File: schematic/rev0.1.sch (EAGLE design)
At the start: 28 parts, among them IC1 L293DD, IC2 L293DD, IC3 L293DD, J1 USB_B_PTH, U1 DS1307Z, Y1 32.768kHz, Y2 16MHz

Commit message: finished routing
Added pinout for bipolar stepper motors, need to source small enough stepper for it.
should read datasheets closer to verify H bridge can run on such little voltage (5V stepper?)
Maybe add more decoupling caps for atmega
maybe add through hole for LED's (so you can mount them)
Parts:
- added C7: 1uF, resistor:C-USC0805
- added IC4: L293D, st-microelectronics:L293D
- added LED2, LED3, LED4: (no value), adafruit:LEDCHIPLED_0805
- added Q1: 600mA/40V, SparkFun-DiscreteSemi:TRANS_NPN-MMBT2222AL
- added R3: 10K, resistor:R-US_R0805
- added R4, R5, R6, R7: 330R, resistor:R-US_R0805
- added S1: (no value), SparkFun-Switches:MOMENTARY-SWITCH-SPST-2-SMD-5.2MM
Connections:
- new net D0: IC1.IN1, U$1.PD2(INT2/RXD1)
- new net D1: IC1.IN2, U$1.PD3(INT3/TXD1)
- new net D10: IC3.IN1, U$1.PB6(OC1B/OC4B/ADC13)
- new net D11: IC3.IN2, U$1.PB7(OC0A/OC1C/RTS)
- new net D12: IC3.IN3, U$1.PD6(T1/ADC9/!OC4D)
- new net D13: IC3.IN4, U$1.PC7(ICP3/CLK0/OC4A)
- new net D4: IC1.IN3, U$1.PD4(ICP1/ADC8)
- new net D5: IC1.IN4, U$1.PC6(OC3A/!OC4A)
- new net D6: IC2.IN1, U$1.PD7(OC4D/ADC10/T0)
- new net D7: IC2.IN2, U$1.PE6(INT.6/AIN0)
- new net D8: IC2.IN3, U$1.PB4(ADC11)
- new net D9: IC2.IN4, U$1.PB5(OC1A/ADC12/!OC4B)
- new net LED_CTRL: Q1.B, U$1.PF7(ADC7(TDI)
- new net N$10: LED2.A, R5.1
- new net N$11: LED3.A, R6.1
- new net N$12: LED4.A, R7.1
- new net N$33: IC4.1A
- new net N$34: IC4.2A
- new net N$35: IC4.3A
- new net N$36: IC4.4A
- new net N$8: C7.1, U$1.UCAP
- new net N$9: LED1.A, R4.1
- net GND: now also C7.2, CN1.GND, J1.GND, J1.SHIELD, LED1.C, LED2.C, LED3.C, LED4.C, S1.1, S1.2, U$1.PE2(!HWB), U$1.UGND
- net N$5: now also Q1.E, R4.2, R5.2, R6.2, R7.2; no longer U1.VCC
- net RST: now also R3.1, S1.3, S1.4, U$1./RESET
- net VCC: now also CN1.PWR, IC1.EN1, IC1.EN2, IC2.EN1, IC2.EN2, IC3.EN1, IC3.EN2, Q1.C, R3.2, U$1.AVCC, U$1.AVCC1, U$1.UVCC, U$1.VBUS, U$1.VCC, U$1.VCC1, U1.VCC
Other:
- moved on the sheet: D2, ISP1, J1, LED1, R1, R2, U$1, Y2

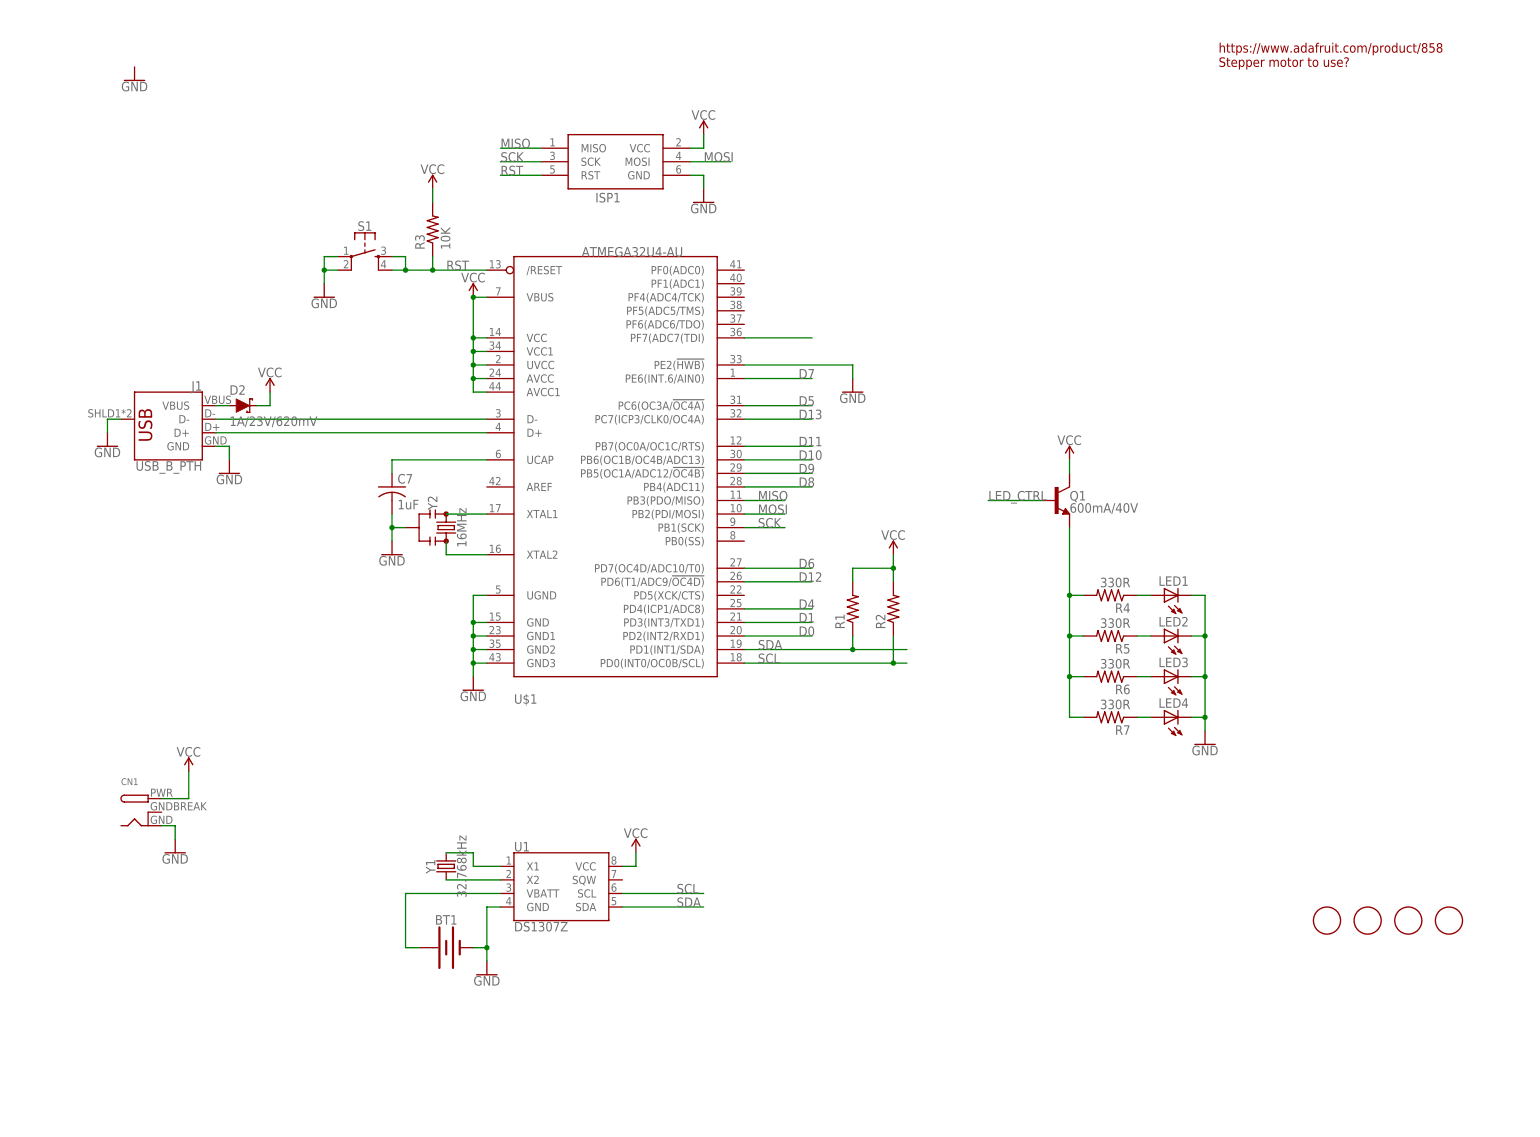
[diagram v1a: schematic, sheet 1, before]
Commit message: closer to done
changed the motor to be driven by 12vin, inserted voltage regulator to have one power supply, constant enable. would like to condence the design a little.
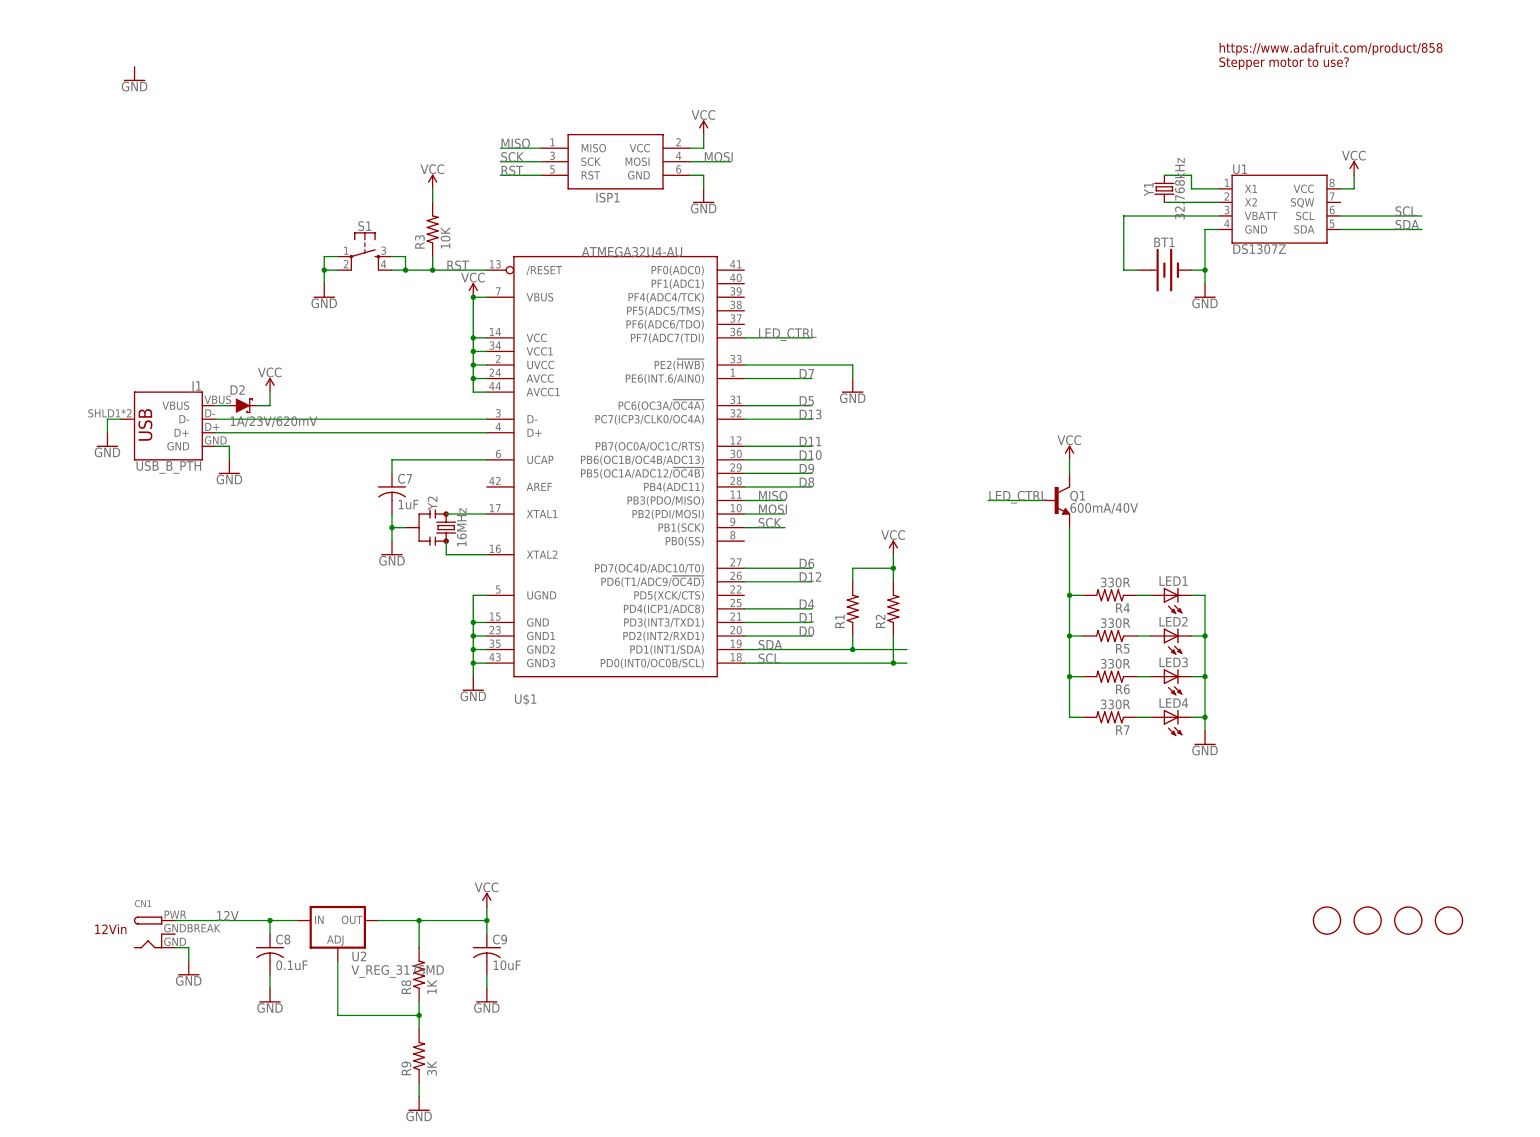
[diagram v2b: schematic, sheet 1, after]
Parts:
- removed IC4: L293D, st-microelectronics:L293D
- added C8: 0.1uF, resistor:C-USC0805
- added C9: 10uF, resistor:C-USC0805
- added R8: 1K, resistor:R-US_R0805
- added R9: 3K, resistor:R-US_R0805
- added U2: V_REG_317SMD, SparkFun-IC-Power:V_REG_317SMD
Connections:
- removed net N$33: IC4.1A
- removed net N$34: IC4.2A
- removed net N$35: IC4.3A
- removed net N$36: IC4.4A
- new net 12V: C1.+, C2.+, C3.+, C4.1, C5.1, C6.1, C8.1, CN1.PWR, IC1.VS, IC2.VS, IC3.VS, U2.IN
- new net N$27: R8.1, R9.2, U2.ADJ
- net GND: now also C8.2, C9.2, R9.1
- net VCC: now also C9.1, R8.2, U2.OUT; no longer C1.+, C2.+, C3.+, C4.1, C5.1, C6.1, CN1.PWR, IC1.VS, IC2.VS, IC3.VS
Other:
- note added: "12Vin"
- moved on the sheet: BT1, C1, C2, C3, C4, C5, C6, CN1, U1, Y1

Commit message: clean up
clean up
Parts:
- added SJ1, SJ2: (no value), jumper:SJ
- renumbered U$1 to U3
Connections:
- new net N$13: SJ2.2, U2.IN
- net 12V: now also SJ1.1, SJ2.1; no longer U2.IN
- net VCC: now also SJ1.2
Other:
- moved on the sheet: C8
